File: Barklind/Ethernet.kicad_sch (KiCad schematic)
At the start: 24 parts, among them U3 W5500, Y1 25MHz

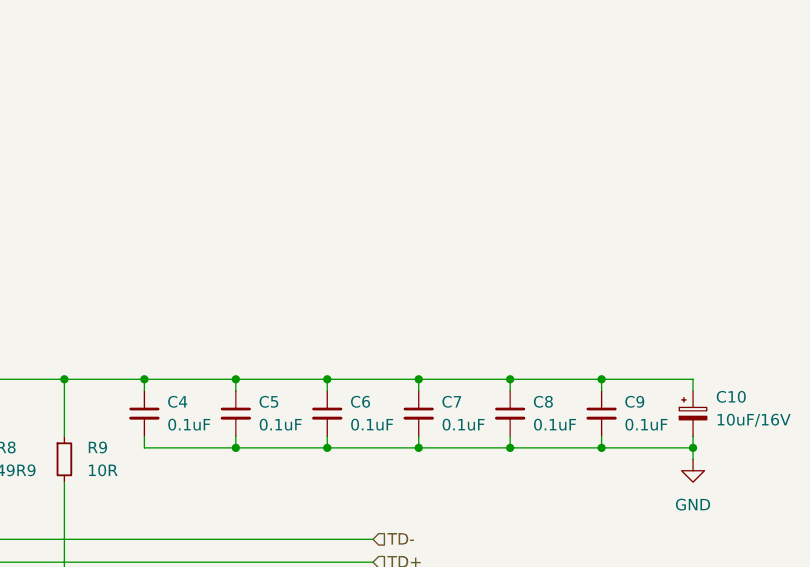
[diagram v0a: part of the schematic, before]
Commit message: Added comment in schematic to test workflow
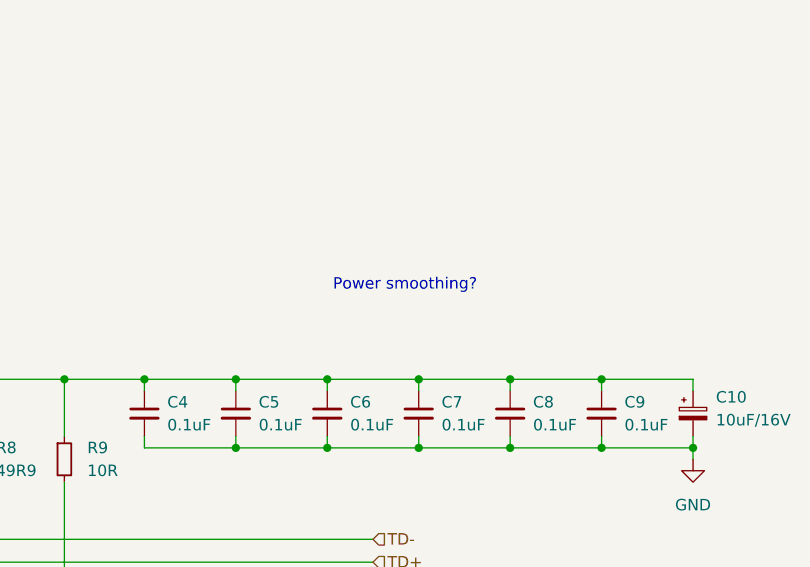
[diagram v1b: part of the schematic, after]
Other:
- note added: "Power smoothing?"
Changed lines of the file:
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@@
+		)
+	)
+	(text "Power smoothing?"
+		(exclude_from_sim no)
+		(at 205.486 60.706 0)
+		(effects
+			(font
+				(size 1.27 1.27)
+			)
 		)
 	)

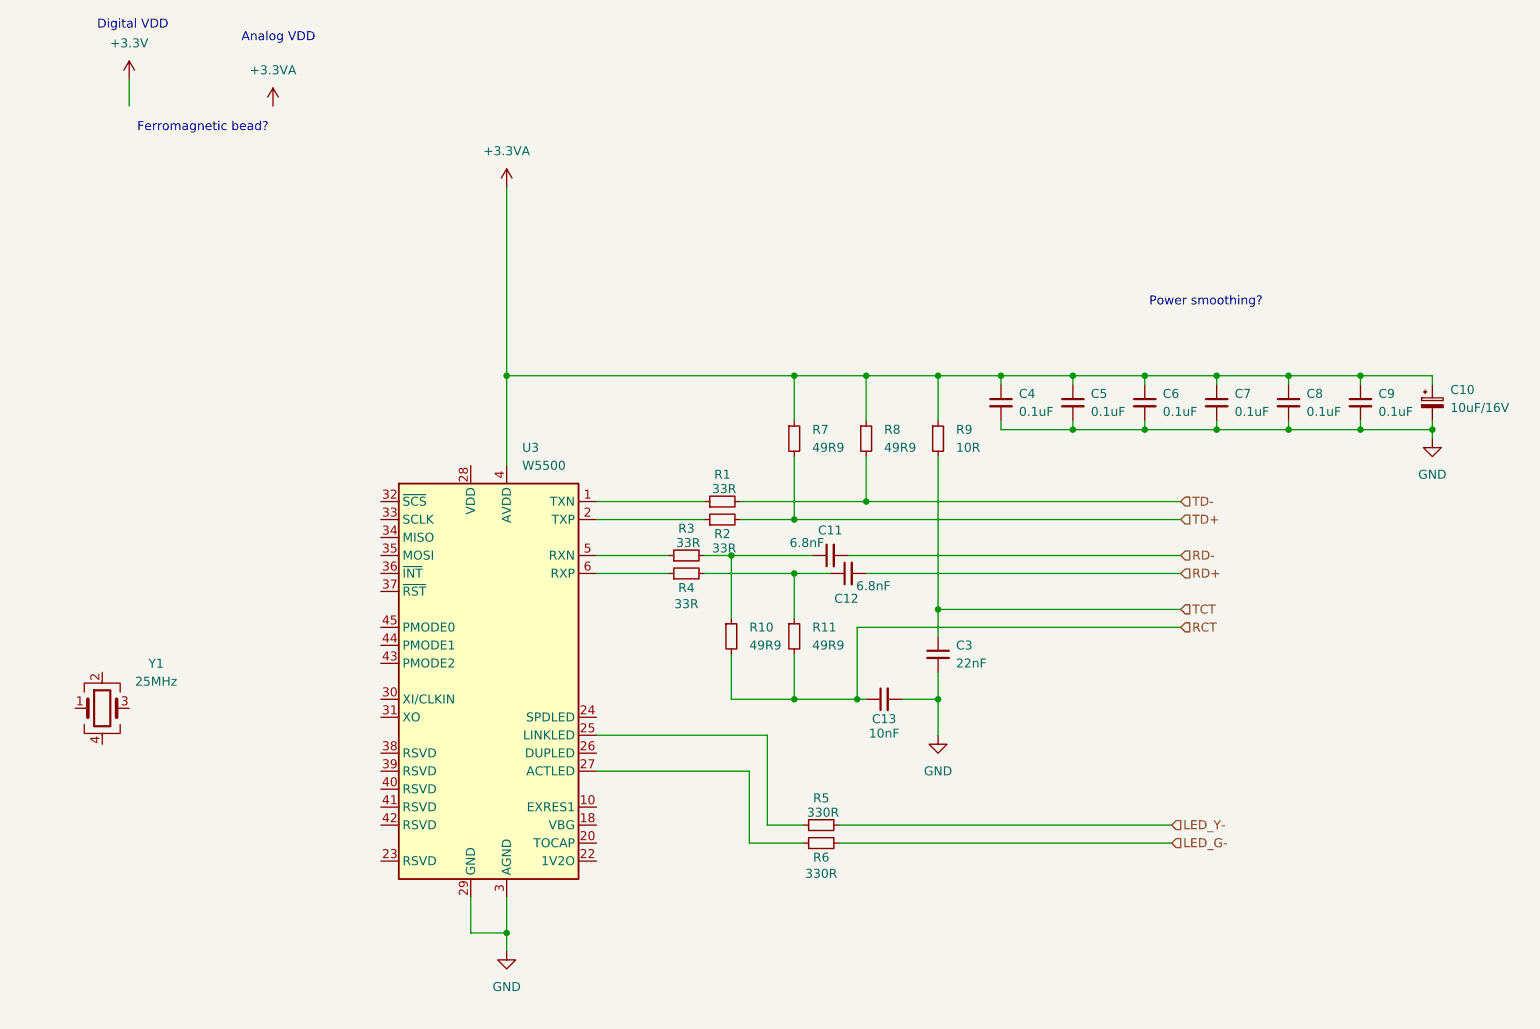
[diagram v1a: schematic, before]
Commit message: Added most components to Ethernet schematic Updated main schematic to add connections to/from ethernet schematic Added connections from ESP32 to Fan driver
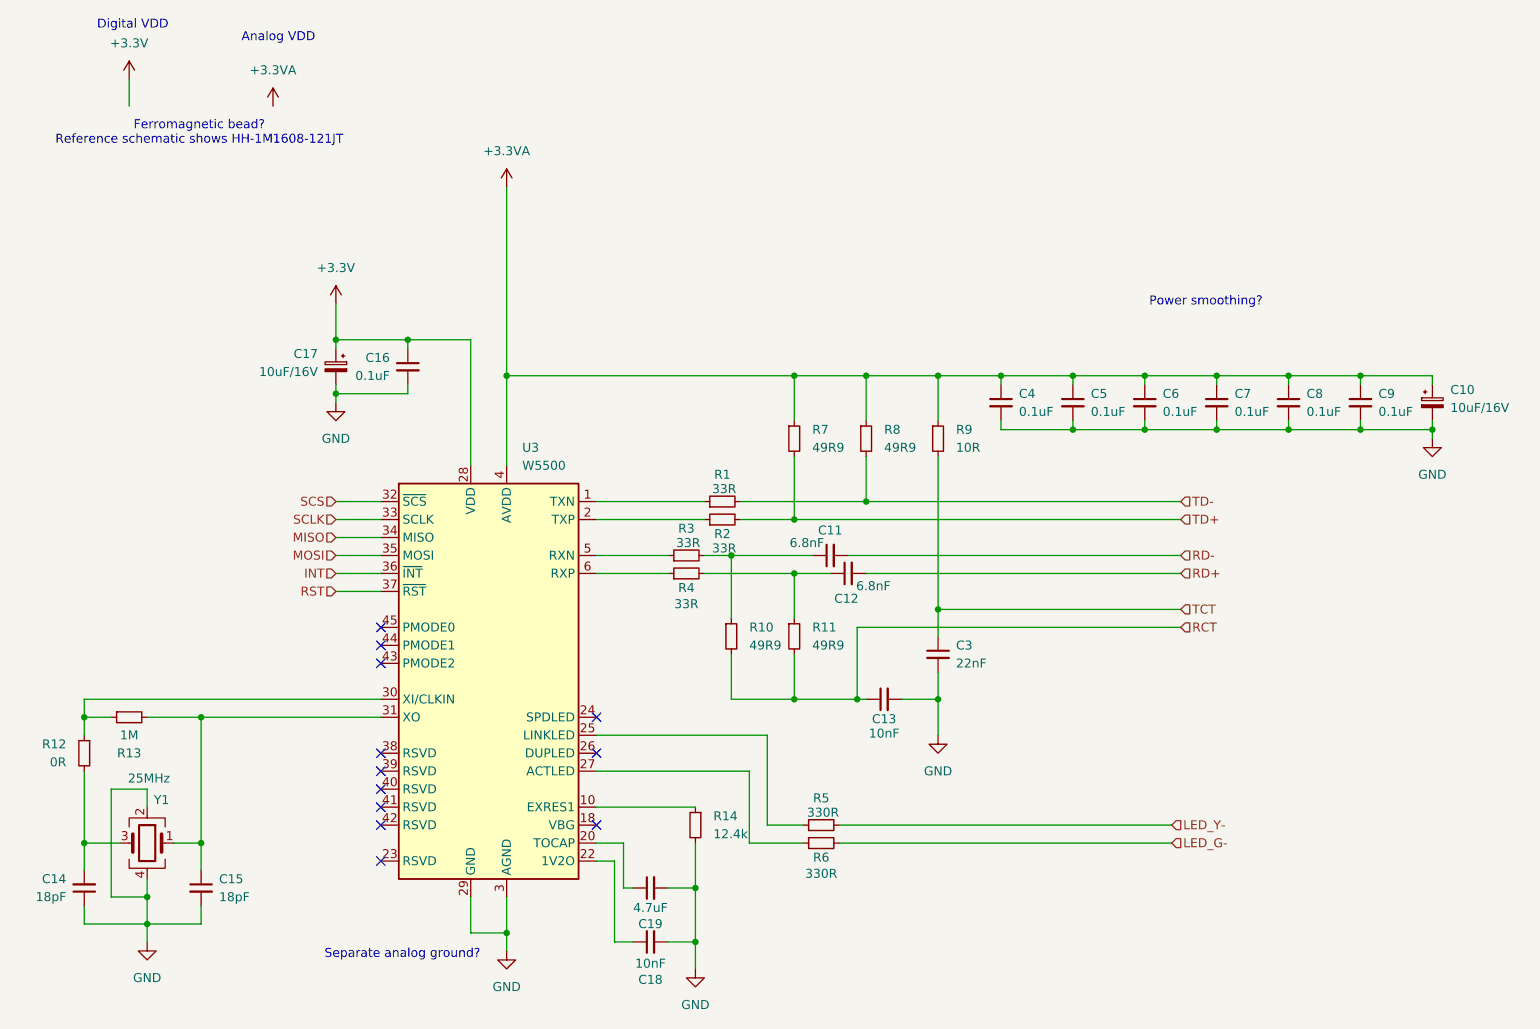
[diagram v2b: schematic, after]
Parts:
- added C14, C15: 18pF, symbol Device:C_Small
- added C16: 0.1uF, symbol Device:C_Small
- added C17: 10uF/16V, symbol Device:C_Polarized_Small
- added C18: 10nF, symbol Device:C_Small
- added C19: 4.7uF, symbol Device:C_Small
- added R12: 0R, symbol Device:R_Small
- added R13: 1M, symbol Device:R_Small
- added R14: 12.4k, symbol Device:R_Small
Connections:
- net +3.3V: now also U3.28 (VDD), C16.1, C17.1
- net GND: now also Y1.2, Y1.4, C14.1, C15.2, C16.2, C17.2, C18.2, C19.2, R14.2
- net at Y1.1: now also U3.31 (XO), C15.1, R13.2
- net at Y1.3: now also C14.2, R12.2
- net at U3.10 (EXRES1): now also R14.1
- net at U3.20 (TOCAP): now also C19.1
- net at U3.22 (1V2O): now also C18.1
- net at U3.30 (XI/CLKIN): now also R12.1, R13.1
- net SCS: now reaches U3.32 (~{SCS})
- net SCLK: now reaches U3.33 (SCLK)
- net MISO: now reaches U3.34 (MISO)
- net MOSI: now reaches U3.35 (MOSI)
- net INT: now reaches U3.36 (~{INT})
- net RST: now reaches U3.37 (~{RST})
- no-connect marks 0 -> 12
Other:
- note added: "Ferromagnetic bead? Reference schematic shows HH-1M1608-121JT"
- note added: "Separate analog ground?"
- note removed: "Ferromagnetic bead?"
- moved on the sheet: Y1

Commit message: Added basic board (with no layout specified) Added additional comments to schematic
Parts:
- R1, R10, R11, R12, R13, R14, R2, R3, R4, R5, R6, R7, R8, R9: footprint (none) -> Resistor_SMD:R_0805_2012Metric
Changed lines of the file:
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@@
 			)
 		)
-		(property "Footprint" ""
+		(property "Footprint" "Resistor_SMD:R_0805_2012Metric"
 			(at 53.34 119.38 0)
 			(effects
@@
 			)
 		)
-		(property "Footprint" ""
+		(property "Footprint" "Resistor_SMD:R_0805_2012Metric"
 			(at 137.16 88.9 0)
 			(effects
@@
 			)
 		)
-		(property "Footprint" ""
+		(property "Footprint" "Resistor_SMD:R_0805_2012Metric"
 			(at 46.99 124.46 0)
 			(effects
@@
 			)
 		)
-		(property "Footprint" ""
+		(property "Footprint" "Resistor_SMD:R_0805_2012Metric"
 			(at 151.13 137.16 0)
 			(effects
@@
 			)
 		)
-		(property "Footprint" ""
+		(property "Footprint" "Resistor_SMD:R_0805_2012Metric"
 			(at 157.48 80.01 0)
 			(effects
@@
 			)
 		)
-		(property "Footprint" ""
+		(property "Footprint" "Resistor_SMD:R_0805_2012Metric"
 			(at 137.16 91.44 0)
 			(effects
@@
 			)
 		)
-		(property "Footprint" ""
+		(property "Footprint" "Resistor_SMD:R_0805_2012Metric"
 			(at 138.43 107.95 0)
 			(effects
@@
 			)
 		)
-		(property "Footprint" ""
+		(property "Footprint" "Resistor_SMD:R_0805_2012Metric"
 			(at 133.35 134.62 0)
 			(effects
@@
 			)
 		)
-		(property "Footprint" ""
+		(property "Footprint" "Resistor_SMD:R_0805_2012Metric"
 			(at 132.08 99.06 0)
 			(effects
@@
 			)
 		)
-		(property "Footprint" ""
+		(property "Footprint" "Resistor_SMD:R_0805_2012Metric"
 			(at 132.08 96.52 0)
 			(effects
@@
 			)
 		)
-		(property "Footprint" ""
+		(property "Footprint" "Resistor_SMD:R_0805_2012Metric"
 			(at 151.13 134.62 0)
 			(effects
@@
 			)
 		)
-		(property "Footprint" ""
+		(property "Footprint" "Resistor_SMD:R_0805_2012Metric"
 			(at 147.32 80.01 0)
 			(effects
@@
 			)
 		)
-		(property "Footprint" ""
+		(property "Footprint" "Resistor_SMD:R_0805_2012Metric"
 			(at 167.64 80.01 0)
 			(effects
@@
 			)
 		)
-		(property "Footprint" ""
+		(property "Footprint" "Resistor_SMD:R_0805_2012Metric"
 			(at 147.32 107.95 0)
 			(effects
